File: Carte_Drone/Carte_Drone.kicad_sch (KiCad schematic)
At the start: 3 parts

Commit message: Ajout empreinte microcontrôleur
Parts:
- U1: footprint (none) -> Librairie_Drone:MODULE_NUCLEO-F303K8
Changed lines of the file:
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@@
 			)
 		)
-		(property "Footprint" ""
+		(property "Footprint" "Librairie_Drone:MODULE_NUCLEO-F303K8"
 			(at 97.79 46.99 0)
 			(effects

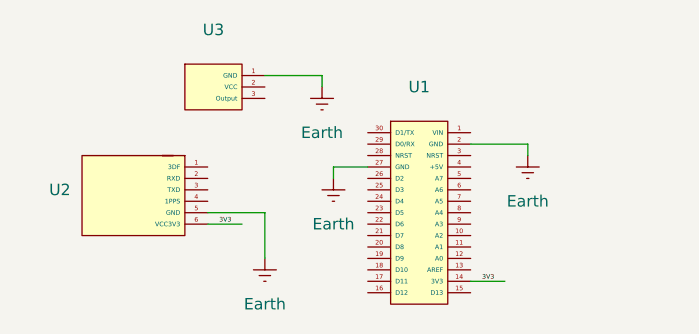
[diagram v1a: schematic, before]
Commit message: Ajout et modifications d'empreintes
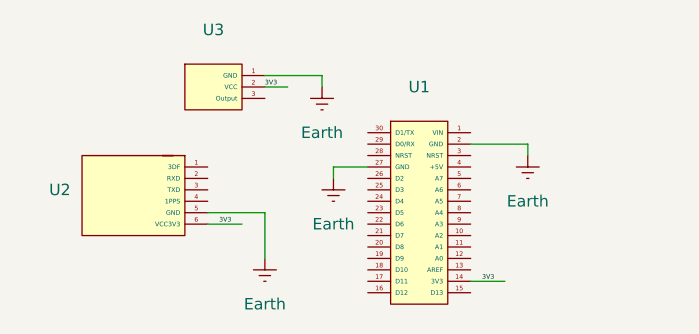
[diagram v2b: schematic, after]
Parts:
- U2: footprint (none) -> Connector_PinSocket_1.00mm:PinSocket_1x06_P1.00mm_Vertical
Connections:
- net 3V3: now also U3.2 (VCC)
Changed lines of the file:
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@@
+	(wire
+		(pts
+			(xy 77.47 45.72) (xy 80.01 45.72)
+		)
+		(stroke
+			(width 0)
+			(type default)
+		)
+	)
 	(wire
 		(pts
@@
 			(width 0)
 			(type default)
+		)
+	)
+	(label "3V3"
+		(at 77.47 45.72 0)
+		(effects
+			(font
+				(size 0.508 0.508)
+			)
+			(justify left bottom)
 		)
 	)
@@
 			)
 		)
-		(property "Footprint" ""
+		(property "Footprint" "Connector_PinSocket_1.00mm:PinSocket_1x06_P1.00mm_Vertical"
 			(at 66.04 52.07 0)
 			(effects

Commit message: Ajout et modifications d'empreintes 2
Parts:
- U2: footprint Connector_PinSocket_1.00mm:PinSocket_1x06_P1.00mm_Vertical -> Connector_PinSocket_1.27mm:PinSocket_1x06_P1.27mm_Vertical
- U3: footprint (none) -> Connector_PinSocket_1.27mm:PinSocket_1x03_P1.27mm_Vertical
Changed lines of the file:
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@@
 			)
 		)
-		(property "Footprint" ""
+		(property "Footprint" "Connector_PinSocket_1.27mm:PinSocket_1x03_P1.27mm_Vertical"
 			(at 69.85 41.91 0)
 			(effects
@@
 			)
 		)
-		(property "Footprint" "Connector_PinSocket_1.00mm:PinSocket_1x06_P1.00mm_Vertical"
+		(property "Footprint" "Connector_PinSocket_1.27mm:PinSocket_1x06_P1.27mm_Vertical"
 			(at 66.04 52.07 0)
 			(effects

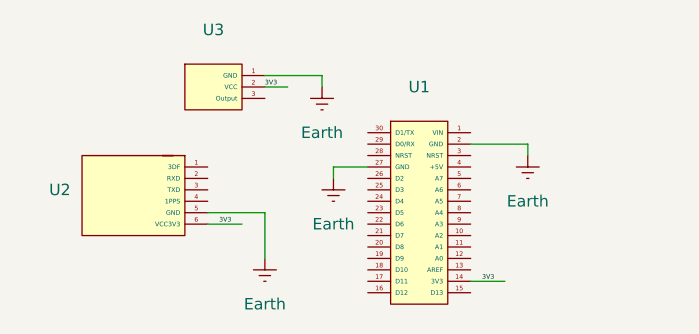
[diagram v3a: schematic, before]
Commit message: Ajout connexion capteur son et microcontrôleur
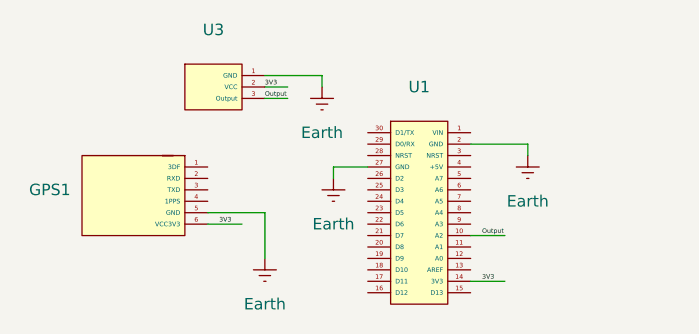
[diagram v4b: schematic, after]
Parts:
- renumbered U2 to GPS1
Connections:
- net Output: now reaches U3.3 (Output)
- net Output: now also U1.10 (A2)
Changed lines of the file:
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@@
+	(wire
+		(pts
+			(xy 100.33 62.23) (xy 104.14 62.23)
+		)
+		(stroke
+			(width 0)
+			(type default)
+		)
+	)
 	(wire
 		(pts
@@
 		(pts
 			(xy 77.47 44.45) (xy 83.82 44.45)
+		)
+		(stroke
+			(width 0)
+			(type default)
+		)
+	)
+	(wire
+		(pts
+			(xy 77.47 46.99) (xy 80.01 46.99)
 		)
 		(stroke
@@
 	(label "3V3"
 		(at 101.6 67.31 0)
+		(effects
+			(font
+				(size 0.508 0.508)
+			)
+			(justify left bottom)
+		)
+	)
+	(label "Output"
+		(at 101.6 62.23 0)
+		(effects
+			(font
+				(size 0.508 0.508)
+			)
+			(justify left bottom)
+		)
+	)
+	(label "Output"
+		(at 77.47 46.99 0)
 		(effects
 			(font
@@
 		(on_board yes)
 		(dnp no)
-		(property "Reference" "U2"
+		(property "Reference" "GPS1"
 			(at 55.88 57.1499 0)
 			(effects
@@
 			(project ""
 				(path "/8b2e4a81-52b6-4667-8a39-1aa7e9632131"
-					(reference "U2")
+					(reference "GPS1")
 					(unit 1)
 				)

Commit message: Ajout d'un composant et de documents
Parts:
- added BLU1: ~, Connector_PinSocket_1.27mm:PinSocket_1x06_P1.27mm_Vertical, symbol Librairie_Drone:HC-05
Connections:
- net 3V3: now also BLU1.2 (VCC)
- net Earth: now also BLU1.3 (GND)
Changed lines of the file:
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@@
+	(wire
+		(pts
+			(xy 102.87 45.72) (xy 102.87 44.45)
+		)
+		(stroke
+			(width 0)
+			(type default)
+		)
+	)
 	(wire
 		(pts
@@
 	(wire
 		(pts
+			(xy 102.87 44.45) (xy 105.41 44.45)
+		)
+		(stroke
+			(width 0)
+			(type default)
+		)
+	)
+	(wire
+		(pts
 			(xy 100.33 52.07) (xy 106.68 52.07)
 		)
@@
 	(wire
 		(pts
+			(xy 102.87 43.18) (xy 105.41 43.18)
+		)
+		(stroke
+			(width 0)
+			(type default)
+		)
+	)
+	(wire
+		(pts
 			(xy 77.47 46.99) (xy 80.01 46.99)
 		)
@@
 			(width 0)
 			(type default)
+		)
+	)
+	(label "3V3"
+		(at 104.14 43.18 0)
+		(effects
+			(font
+				(size 0.508 0.508)
+			)
+			(justify left bottom)
 		)
 	)
@@
 	)
 	(symbol
+		(lib_id "power:Earth")
+		(at 102.87 45.72 0)
+		(unit 1)
+		(exclude_from_sim no)
+		(in_bom yes)
+		(on_board yes)
+		(dnp no)
+		(property "Reference" "#PWR05"
+			(at 102.87 52.07 0)
+			(effects
+				(font
+					(size 1.27 1.27)
+				)
+				(hide yes)
+			)
+		)
+		(property "Value" "Earth"
+			(at 102.87 49.53 0)
+			(effects
+				(font
+					(size 1.27 1.27)
+				)
+			)
+		)
+		(property "Footprint" ""
+			(at 102.87 45.72 0)
+			(effects
+				(font
+					(size 1.27 1.27)
+				)
+				(hide yes)
+			)
+		)
+		(property "Datasheet" "~"
+			(at 102.87 45.72 0)
+			(effects
+				(font
+					(size 1.27 1.27)
+				)
+				(hide yes)
+			)
+		)
+		(property "Description" "Power symbol creates a global label with name \"Earth\""
+			(at 102.87 45.72 0)
+			(effects
+				(font
+					(size 1.27 1.27)
+				)
+				(hide yes)
+			)
+		)
+		(pin "1"
+		)
+		(instances
+			(project "Carte_Drone"
+				(path "/8b2e4a81-52b6-4667-8a39-1aa7e9632131"
+					(reference "#PWR05")
+					(unit 1)
+				)
+			)
+		)
+	)
+	(symbol
 		(lib_id "Librairie_Drone:Analog_Sound_Sensor")
 		(at 69.85 41.91 0)
@@
 					(unit 1)
 				)
+			)
+		)
+	)
+	(symbol
+		(lib_id "Librairie_Drone:HC-05")
+		(at 109.22 39.37 0)
+		(unit 1)
+		(exclude_from_sim no)
+		(in_bom yes)
+		(on_board yes)
+		(dnp no)
+		(fields_autoplaced yes)
+		(property "Reference" "BLU1"
+			(at 118.11 44.4499 0)
+			(effects
+				(font
+					(size 1.27 1.27)
+				)
+				(justify left)
+			)
+		)
+		(property "Value" "~"
+			(at 118.11 46.355 0)
+			(effects
+				(font
+					(size 1.27 1.27)
+				)
+				(justify left)
+			)
+		)
+		(property "Footprint" "Connector_PinSocket_1.27mm:PinSocket_1x06_P1.27mm_Vertical"
+			(at 109.22 39.37 0)
+			(effects
+				(font
+					(size 1.27 1.27)
+				)
+				(hide yes)
+			)
+		)
+		(property "Datasheet" ""
+			(at 109.22 39.37 0)
+			(effects
+				(font
+					(size 1.27 1.27)
+				)
+				(hide yes)
+			)
+		)
+		(property "Description" ""
+			(at 109.22 39.37 0)
+			(effects
+				(font
+					(size 1.27 1.27)
+				)
+				(hide yes)
+			)
+		)
+		(pin "1"
+		)
+		(pin "5"
+		)
+		(pin "6"
+		)
+		(pin "2"
+		)
+		(pin "4"
+		)
+		(pin "3"
+		)
+		(instances
+			(project ""
+				(path "/8b2e4a81-52b6-4667-8a39-1aa7e9632131"
+					(reference "BLU1")
+					(unit 1)
+				)

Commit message: Fin de la création de la carte
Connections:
- net TXB: now reaches BLU1.4 (TXD)
- net TXB: now also U1.24 (D4)
- net RXB: now reaches BLU1.5 (RXD)
- net RXB: now also U1.23 (D5)
- net TXG: now reaches U1.29 (D0/RX)
- net TXG: now also GPS1.3 (TXD)
- net RXG: now reaches U1.30 (D1/TX)
- net RXG: now also GPS1.2 (RXD)
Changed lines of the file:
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@@
-	(wire
-		(pts
-			(xy 102.87 45.72) (xy 102.87 44.45)
-		)
-		(stroke
-			(width 0)
-			(type default)
-		)
-	)
 	(wire
 		(pts
@@
 	(wire
 		(pts
+			(xy 86.36 59.69) (xy 88.9 59.69)
+		)
+		(stroke
+			(width 0)
+			(type default)
+		)
+	)
+	(wire
+		(pts
 			(xy 100.33 67.31) (xy 104.14 67.31)
 		)
@@
 	(wire
 		(pts
-			(xy 102.87 44.45) (xy 105.41 44.45)
+			(xy 97.79 44.45) (xy 105.41 44.45)
+		)
+		(stroke
+			(width 0)
+			(type default)
+		)
+	)
+	(wire
+		(pts
+			(xy 71.12 57.15) (xy 74.93 57.15)
+		)
+		(stroke
+			(width 0)
+			(type default)
+		)
+	)
+	(wire
+		(pts
+			(xy 86.36 50.8) (xy 88.9 50.8)
+		)
+		(stroke
+			(width 0)
+			(type default)
+		)
+	)
+	(wire
+		(pts
+			(xy 86.36 58.42) (xy 88.9 58.42)
 		)
 		(stroke
@@
 	(wire
 		(pts
+			(xy 101.6 45.72) (xy 105.41 45.72)
+		)
+		(stroke
+			(width 0)
+			(type default)
+		)
+	)
+	(wire
+		(pts
 			(xy 100.33 62.23) (xy 104.14 62.23)
 		)
@@
 	(wire
 		(pts
+			(xy 71.12 55.88) (xy 74.93 55.88)
+		)
+		(stroke
+			(width 0)
+			(type default)
+		)
+	)
+	(wire
+		(pts
+			(xy 101.6 46.99) (xy 105.41 46.99)
+		)
+		(stroke
+			(width 0)
+			(type default)
+		)
+	)
+	(wire
+		(pts
 			(xy 106.68 52.07) (xy 106.68 53.34)
 		)
@@
 		(pts
 			(xy 85.09 55.88) (xy 85.09 54.61)
+		)
+		(stroke
+			(width 0)
+			(type default)
+		)
+	)
+	(wire
+		(pts
+			(xy 86.36 52.07) (xy 88.9 52.07)
 		)
 		(stroke
@@
 		)
 	)
+	(label "RXG"
+		(at 72.39 55.88 0)
+		(effects
+			(font
+				(size 0.508 0.508)
+			)
+			(justify left bottom)
+		)
+	)
+	(label "RXB"
+		(at 102.87 46.99 0)
+		(effects
+			(font
+				(size 0.508 0.508)
+			)
+			(justify left bottom)
+		)
+	)
 	(label "3V3"
 		(at 101.6 67.31 0)
@@
 		)
 	)
+	(label "TXB"
+		(at 87.63 58.42 0)
+		(effects
+			(font
+				(size 0.508 0.508)
+			)
+			(justify left bottom)
+		)
+	)
+	(label "RXB"
+		(at 87.63 59.69 0)
+		(effects
+			(font
+				(size 0.508 0.508)
+			)
+			(justify left bottom)
+		)
+	)
+	(label "TXG"
+		(at 72.39 57.15 0)
+		(effects
+			(font
+				(size 0.508 0.508)
+			)
+			(justify left bottom)
+		)
+	)
+	(label "TXB"
+		(at 102.87 45.72 0)
+		(effects
+			(font
+				(size 0.508 0.508)
+			)
+			(justify left bottom)
+		)
+	)
 	(label "3V3"
 		(at 72.39 60.96 0)
+		(effects
+			(font
+				(size 0.508 0.508)
+			)
+			(justify left bottom)
+		)
+	)
+	(label "RXG"
+		(at 87.63 50.8 0)
+		(effects
+			(font
+				(size 0.508 0.508)
+			)
+			(justify left bottom)
+		)
+	)
+	(label "TXG"
+		(at 87.63 52.07 0)
 		(effects
 			(font
@@
 	(symbol
 		(lib_id "power:Earth")
-		(at 102.87 45.72 0)
+		(at 97.79 44.45 0)
 		(unit 1)
 		(exclude_from_sim no)
@@
 		(dnp no)
 		(property "Reference" "#PWR05"
-			(at 102.87 52.07 0)
+			(at 97.79 50.8 0)
 			(effects
 				(font
@@
 		)
 		(property "Value" "Earth"
-			(at 102.87 49.53 0)
+			(at 97.79 48.26 0)
 			(effects
 				(font
@@
 		)
 		(property "Footprint" ""
-			(at 102.87 45.72 0)
+			(at 97.79 44.45 0)
 			(effects
 				(font
@@
 		)
 		(property "Datasheet" "~"
-			(at 102.87 45.72 0)
+			(at 97.79 44.45 0)
 			(effects
 				(font
@@
 		)
 		(property "Description" "Power symbol creates a global label with name \"Earth\""
-			(at 102.87 45.72 0)
-			(effects
-				(font
+			(at 97.79 44.45 0)
+			(effects
+				(font
